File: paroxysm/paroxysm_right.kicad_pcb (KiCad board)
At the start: 2 copper layers, 117.5 x 89.9 mm, 19 parts, among them SW10 SW_Push, SW11 SW_Push, SW12 SW_Push, SW14 SW_Push, SW15 SW_Push, SW16 SW_Push, SW17 SW_Push, SW18 SW_Push, SW20 SW_Push, SW21 SW_Push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

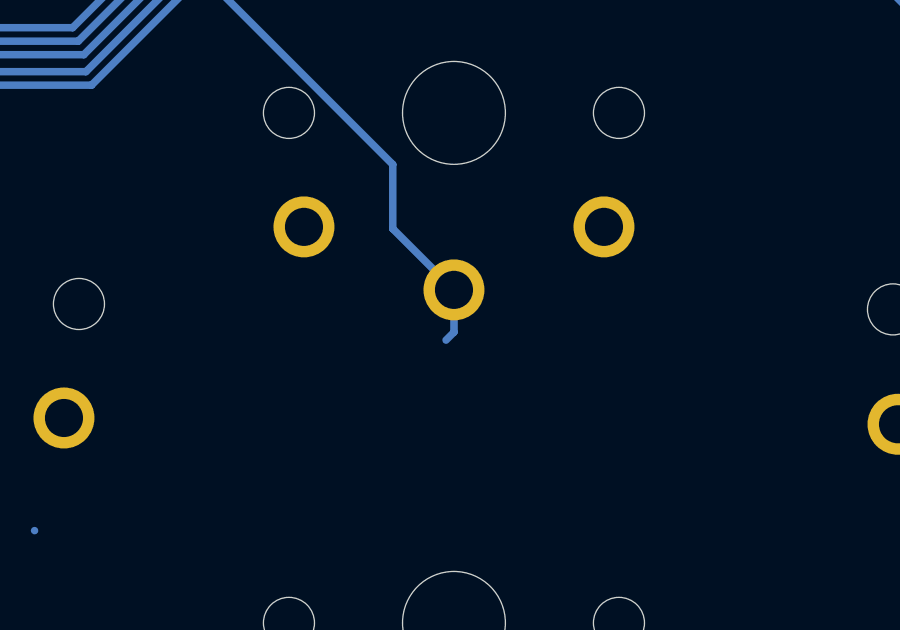
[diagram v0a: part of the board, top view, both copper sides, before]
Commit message: Remove Sweep34
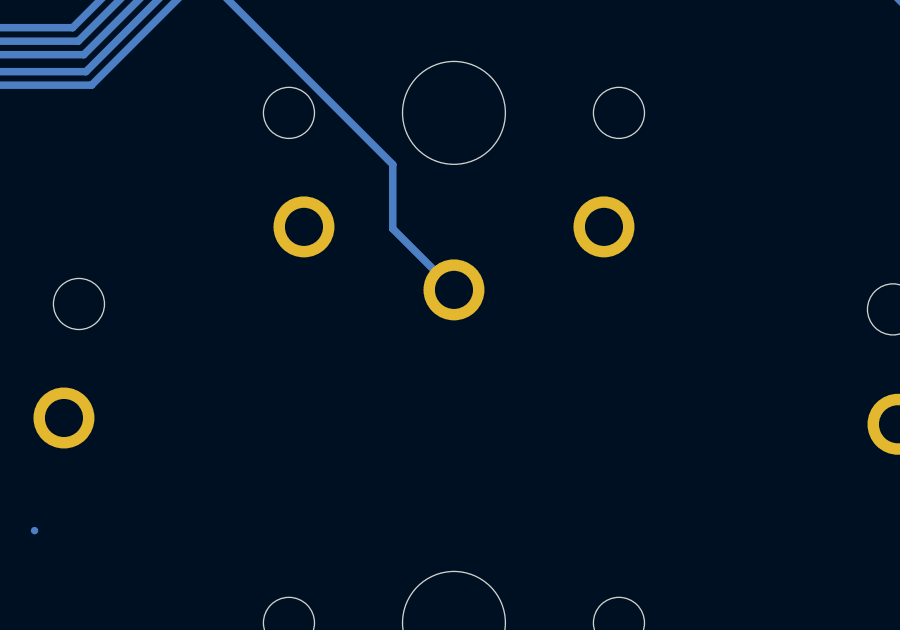
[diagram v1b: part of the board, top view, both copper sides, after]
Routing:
- net Switch8: track 96.2 -> 94.4 mm
